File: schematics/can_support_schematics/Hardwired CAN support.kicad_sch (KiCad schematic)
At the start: 35 parts, among them J1 Conn_01x05_Female, J2 Conn_01x05_Male, J3 Conn_01x05_Male, J4 Screw_Terminal_01x04, J5 Screw_Terminal_01x02, J6 Screw_Terminal_01x02, J7 Screw_Terminal_01x02, Q1 MMBF170, SW1 SW_DIP_x04, U1 SPST_POWER_RELAY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

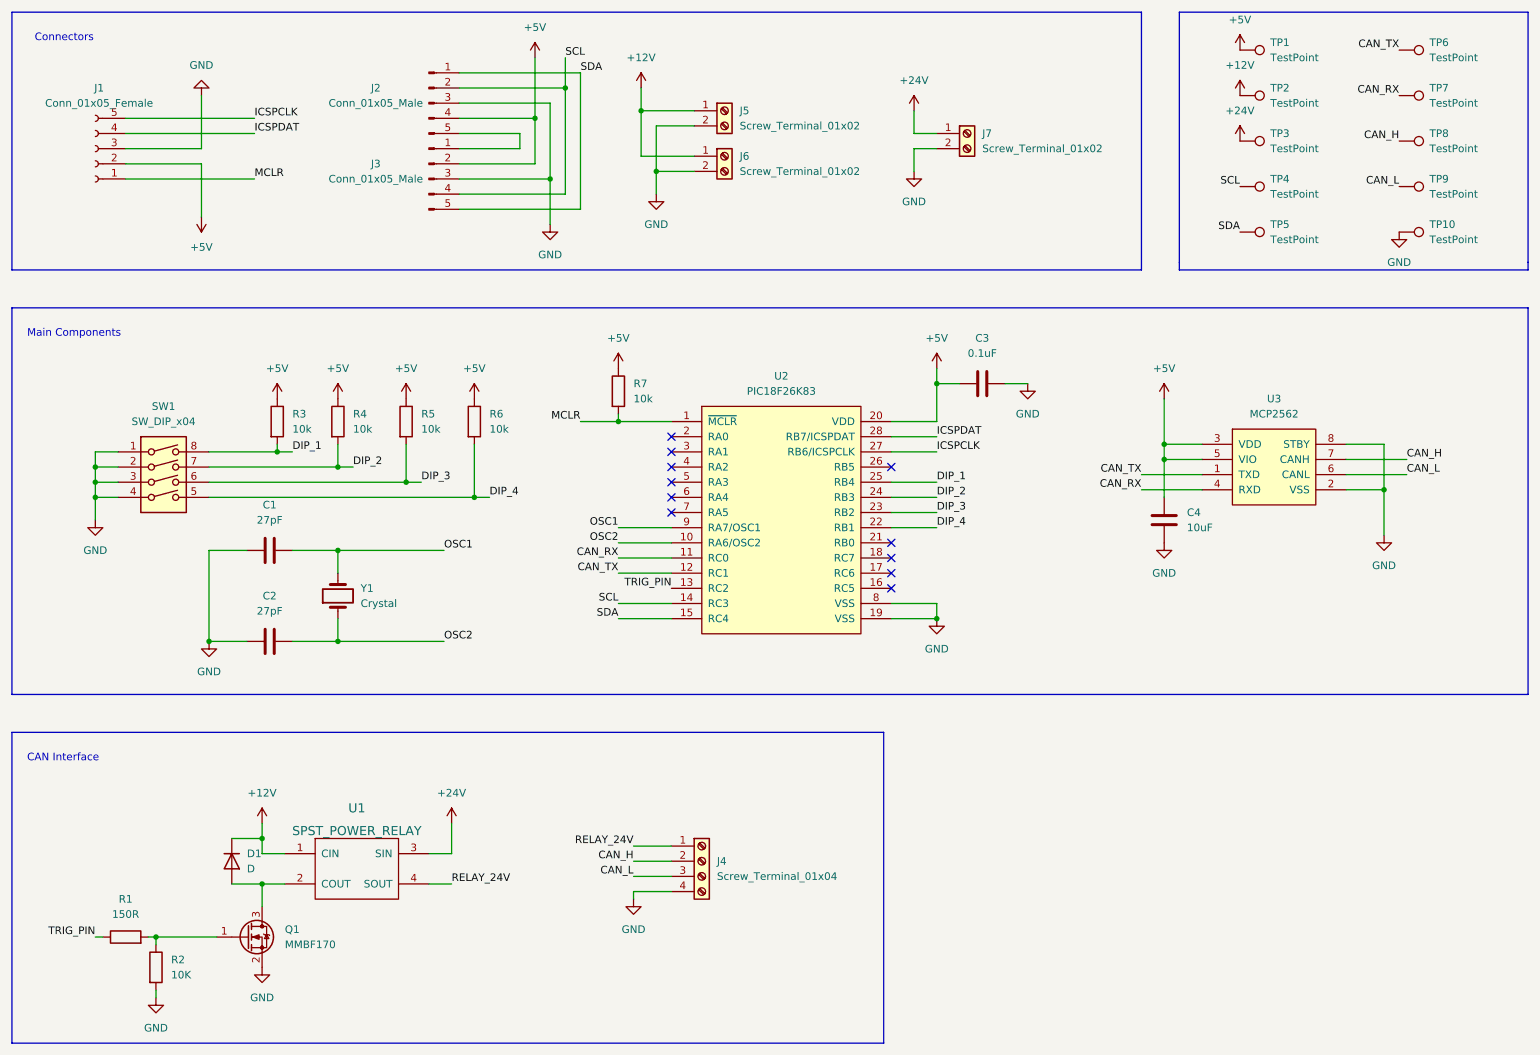
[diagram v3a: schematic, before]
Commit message: Updated recommended changes to PCB
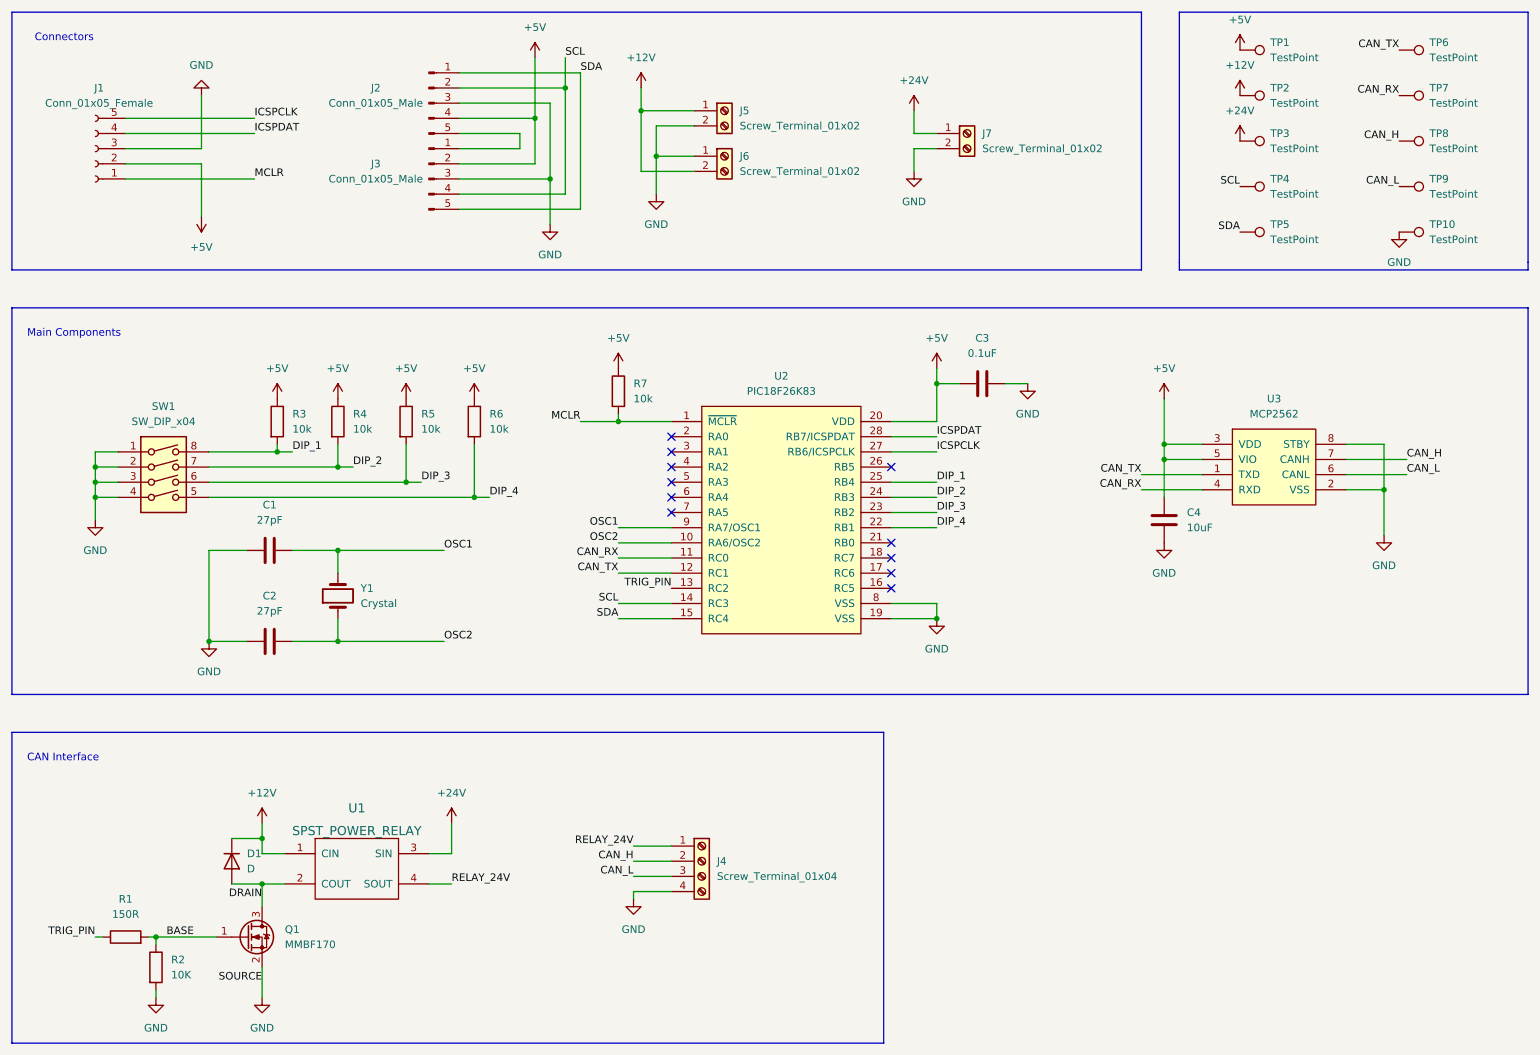
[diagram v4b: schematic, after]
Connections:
- net +12V: now also J6.2 (Pin_2); no longer J6.1 (Pin_1)
- net GND: now also J6.1 (Pin_1); no longer J6.2 (Pin_2)
- net BASE: now reaches Q1.1 (G), R1.2, R2.1
- net DRAIN: now reaches D1.2 (A), Q1.3 (D), U1.2 (COUT)
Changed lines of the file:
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@@
   (junction (at 78.74 120.65) (diameter 0) (color 0 0 0 0)
   )
-  (junction (at 132.08 41.91) (diameter 0) (color 0 0 0 0)
+  (junction (at 132.08 39.37) (diameter 0) (color 0 0 0 0)
   )
   (junction (at 125.73 83.82) (diameter 0) (color 0 0 0 0)
@@
     (stroke (width 0) (type default) (color 0 0 0 0))
   )
+  (wire (pts (xy 132.08 39.37) (xy 138.43 39.37))
+    (stroke (width 0) (type default) (color 0 0 0 0))
+  )
   (wire (pts (xy 99.06 43.18) (xy 114.3 43.18))
     (stroke (width 0) (type default) (color 0 0 0 0))
@@
     (stroke (width 0) (type default) (color 0 0 0 0))
   )
-  (wire (pts (xy 132.08 41.91) (xy 132.08 45.72))
+  (wire (pts (xy 132.08 34.29) (xy 132.08 39.37))
     (stroke (width 0) (type default) (color 0 0 0 0))
   )
@@
     (stroke (width 0) (type default) (color 0 0 0 0))
   )
+  (wire (pts (xy 129.54 31.75) (xy 129.54 41.91))
+    (stroke (width 0) (type default) (color 0 0 0 0))
+  )
   (wire (pts (xy 48.26 170.18) (xy 58.42 170.18))
     (stroke (width 0) (type default) (color 0 0 0 0))
@@
     (stroke (width 0) (type default) (color 0 0 0 0))
   )
-  (wire (pts (xy 129.54 39.37) (xy 138.43 39.37))
-    (stroke (width 0) (type default) (color 0 0 0 0))
-  )
   (wire (pts (xy 138.43 34.29) (xy 132.08 34.29))
     (stroke (width 0) (type default) (color 0 0 0 0))
@@
     (stroke (width 0) (type default) (color 0 0 0 0))
   )
-  (wire (pts (xy 132.08 41.91) (xy 138.43 41.91))
+  (wire (pts (xy 129.54 41.91) (xy 138.43 41.91))
     (stroke (width 0) (type default) (color 0 0 0 0))
   )
@@
     (stroke (width 0) (type default) (color 0 0 0 0))
   )
+  (wire (pts (xy 66.04 180.34) (xy 66.04 175.26))
+    (stroke (width 0) (type default) (color 0 0 0 0))
+  )
   (wire (pts (xy 125.73 114.3) (xy 134.62 114.3))
     (stroke (width 0) (type default) (color 0 0 0 0))
@@
     (stroke (width 0) (type default) (color 0 0 0 0))
   )
-  (wire (pts (xy 129.54 31.75) (xy 129.54 39.37))
-    (stroke (width 0) (type default) (color 0 0 0 0))
-  )
   (polyline (pts (xy 24.13 15.24) (xy 24.13 58.42))
     (stroke (width 0) (type default) (color 0 0 0 0))
@@
     (stroke (width 0) (type default) (color 0 0 0 0))
   )
+  (wire (pts (xy 132.08 39.37) (xy 132.08 45.72))
+    (stroke (width 0) (type default) (color 0 0 0 0))
+  )
   (wire (pts (xy 114.3 30.48) (xy 99.06 30.48))
     (stroke (width 0) (type default) (color 0 0 0 0))
@@
     (stroke (width 0) (type default) (color 0 0 0 0))
   )
-  (wire (pts (xy 132.08 34.29) (xy 132.08 41.91))
-    (stroke (width 0) (type default) (color 0 0 0 0))
-  )
   (wire (pts (xy 128.27 162.56) (xy 128.27 163.83))
     (stroke (width 0) (type default) (color 0 0 0 0))
@@
     (effects (font (size 1.27 1.27)) (justify right bottom))
   )
+  (label "SOURCE" (at 66.04 177.8 180)
+    (effects (font (size 1.27 1.27)) (justify right bottom))
+  )
   (label "ICSPDAT" (at 64.77 35.56 0)
     (effects (font (size 1.27 1.27)) (justify left bottom))
@@
     (effects (font (size 1.27 1.27)) (justify right bottom))
   )
+  (label "BASE" (at 54.61 170.18 180)
+    (effects (font (size 1.27 1.27)) (justify right bottom))
+  )
   (label "OSC1" (at 96.52 105.41 0)
     (effects (font (size 1.27 1.27)) (justify left bottom))
@@
   )
   (label "CAN_TX" (at 256.54 21.59 180)
+    (effects (font (size 1.27 1.27)) (justify right bottom))
+  )
+  (label "DRAIN" (at 66.04 163.83 180)
     (effects (font (size 1.27 1.27)) (justify right bottom))
   )
@@
     (pin "1")
   )
-  (symbol (lib_id "power:GND") (at 66.04 175.26 0) (unit 1)
-    (in_bom yes) (on_board yes) (fields_autoplaced)
-    (property "Reference" "#PWR0102" (id 0) (at 66.04 181.61 0)
-      (effects (font (size 1.27 1.27)) hide)
-    )
-    (property "Value" "GND" (id 1) (at 66.04 180.34 0))
-    (property "Footprint" "" (id 2) (at 66.04 175.26 0)
-      (effects (font (size 1.27 1.27)) hide)
-    )
-    (property "Datasheet" "" (id 3) (at 66.04 175.26 0)
-      (effects (font (size 1.27 1.27)) hide)
-    )
+  (symbol (lib_id "power:GND") (at 66.04 180.34 0) (unit 1)
+    (in_bom yes) (on_board yes) (fields_autoplaced)
+    (property "Reference" "#PWR0102" (id 0) (at 66.04 186.69 0)
+      (effects (font (size 1.27 1.27)) hide)
+    )
+    (property "Value" "GND" (id 1) (at 66.04 185.42 0))
+    (property "Footprint" "" (id 2) (at 66.04 180.34 0)
+      (effects (font (size 1.27 1.27)) hide)
+    )
+    (property "Datasheet" "" (id 3) (at 66.04 180.34 0)
+      (effects (font (size 1.27 1.27)) hide)
+    )

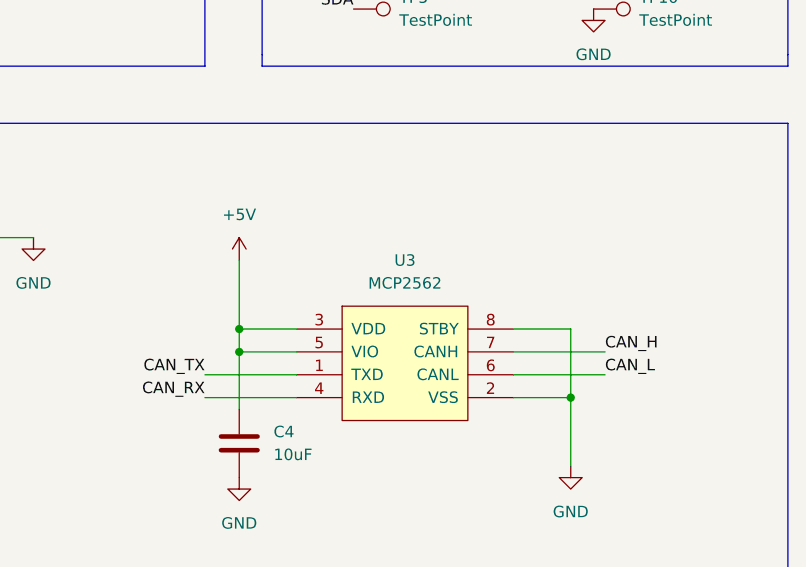
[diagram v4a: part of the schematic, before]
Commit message: Updated name of CAN transceiver
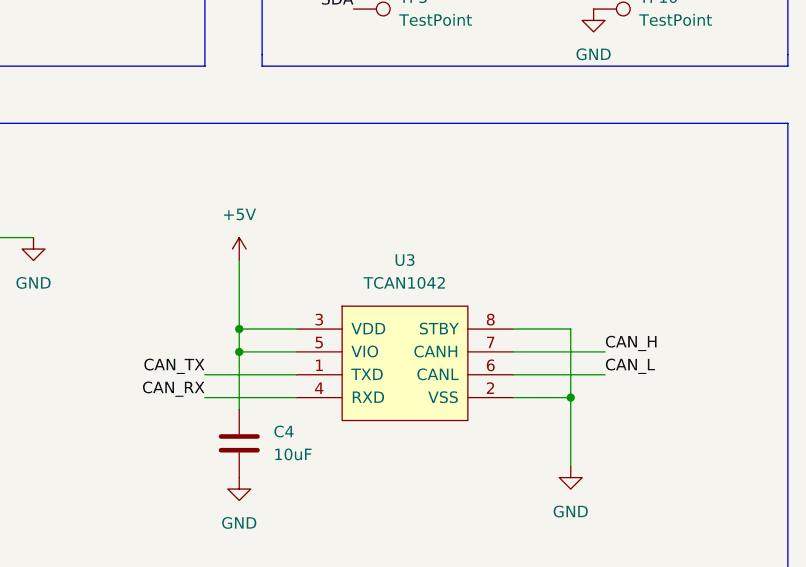
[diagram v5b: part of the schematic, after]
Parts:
- U3: value MCP2562 -> TCAN1042
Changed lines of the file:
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@@
     (in_bom yes) (on_board yes) (fields_autoplaced)
     (property "Reference" "U3" (id 0) (at 235.585 80.01 0))
-    (property "Value" "MCP2562" (id 1) (at 235.585 82.55 0))
+    (property "Value" "TCAN1042" (id 1) (at 235.585 82.55 0))
     (property "Footprint" "Package_SO:SOIC-8_3.9x4.9mm_P1.27mm" (id 2) (at 236.22 87.63 0)
       (effects (font (size 1.27 1.27)) hide)
@@
     )
     (path "/51834992-4e36-4810-91ec-776d460d8f8b"
-      (reference "U3") (unit 1) (value "MCP2562") (footprint "Package_SO:SOIC-8_3.9x4.9mm_P1.27mm")
+      (reference "U3") (unit 1) (value "TCAN1042") (footprint "Package_SO:SOIC-8_3.9x4.9mm_P1.27mm")
     )
     (path "/cda475d1-1c23-4980-8804-c9de5ce42a7e"
